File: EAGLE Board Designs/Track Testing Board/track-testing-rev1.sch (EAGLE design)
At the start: 9 parts, among them J1 CONNECTOR-4_μF_S_RA_, U1 VOLTAGE_REGULATOR_SOT-23-5_5V, U2 VOLTAGE_REFERENCE_SOIC-8_10V

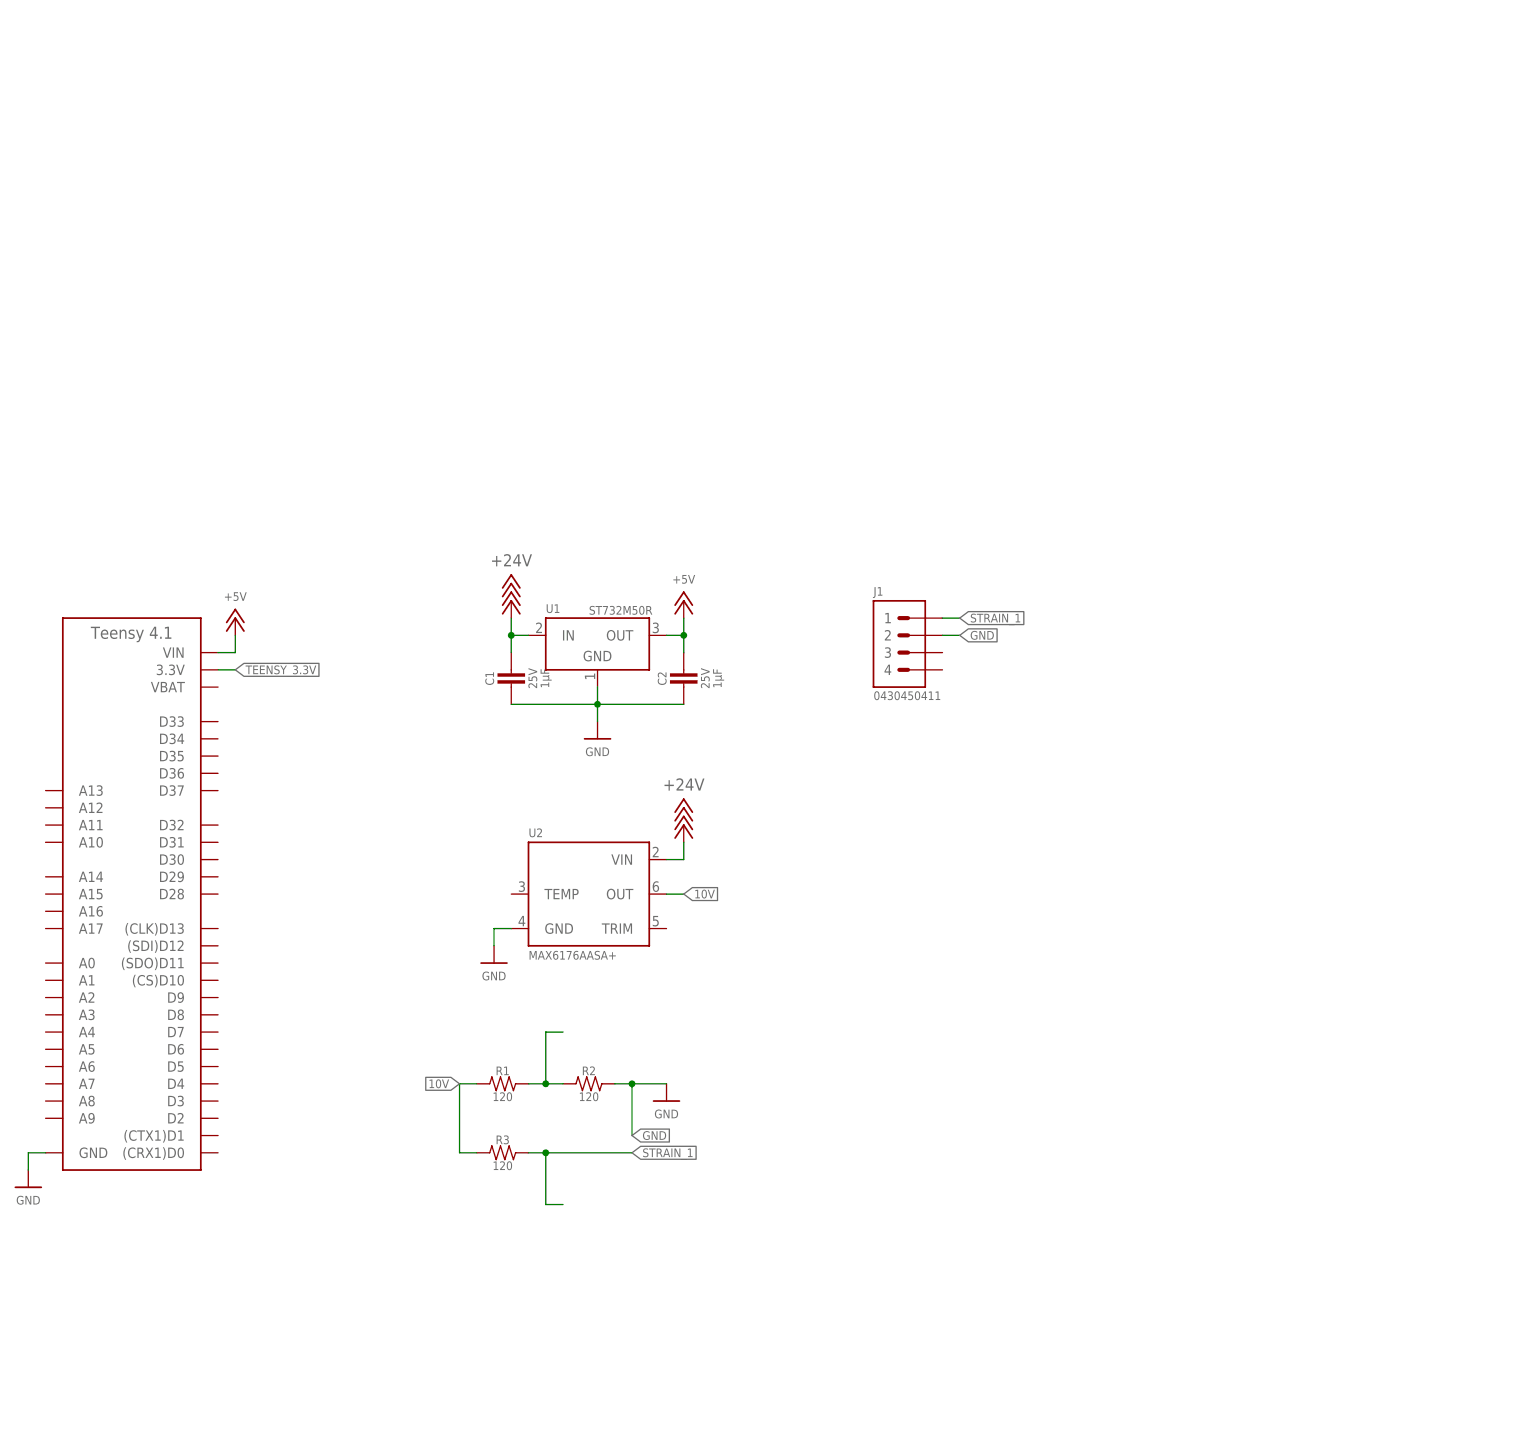
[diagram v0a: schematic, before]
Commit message: enough for two strain gauges
waiting to find datasheet on infrared sensors.
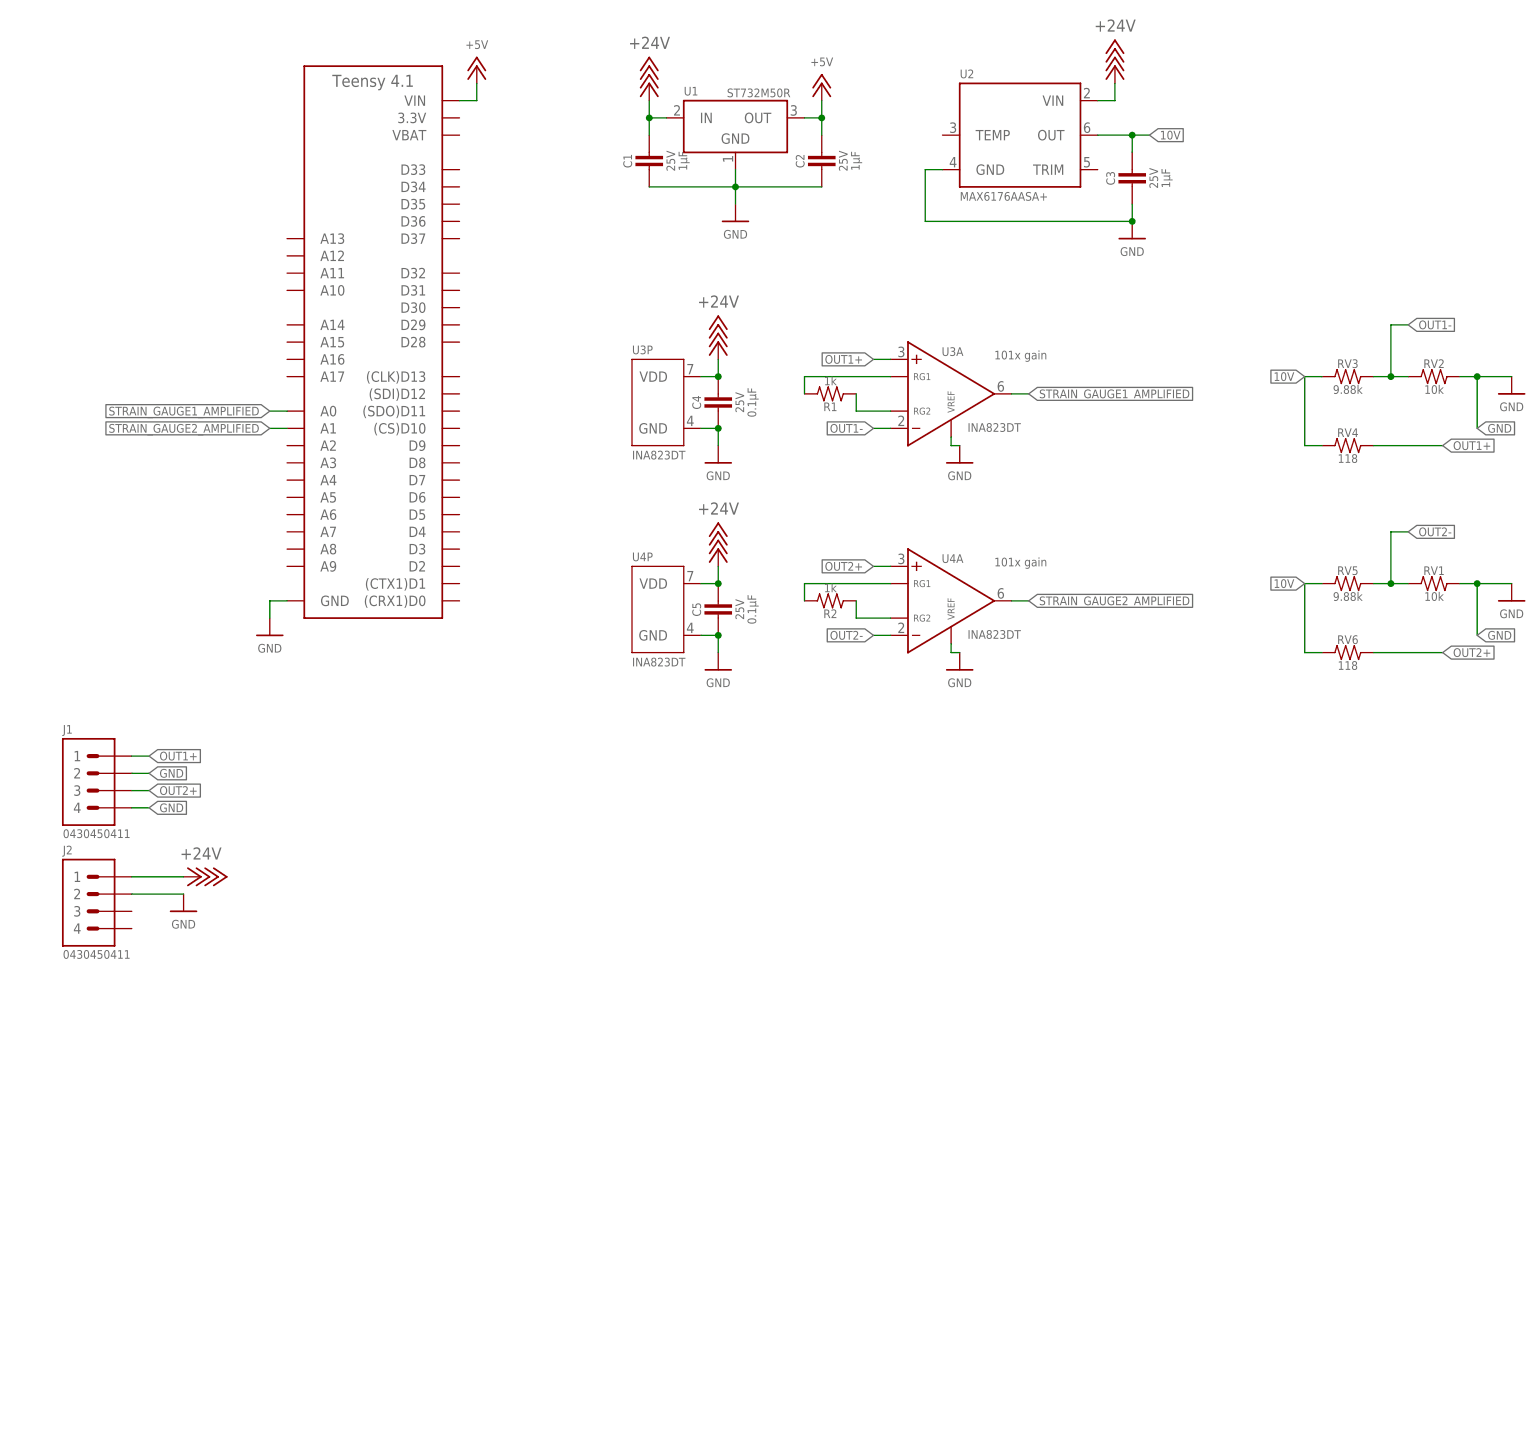
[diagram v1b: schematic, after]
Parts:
- removed R3: RESISTOR_0603_120, HyTechDevices:RESISTOR_0603_120
- added C3: CAPACITOR_0603_25V_1UF, HyTechDevices:CAPACITOR_0603_25V_1UF
- added C4, C5: CAPACITOR_0603_25V_0.1UF, HyTechDevices:CAPACITOR_0603_25V_0.1UF
- added J2: CONNECTOR-4_μF_S_RA_, HyTechDevices:CONNECTOR-4_μF_S_RA_
- added RV1, RV2: 10k, HyTechDevices:RESISTOR_VALUE
- added RV3, RV5: 9.88k, HyTechDevices:RESISTOR_VALUE
- added RV4, RV6: 118, HyTechDevices:RESISTOR_VALUE
- added U3, U4: INA823DT, HyTechDevices:INA823DT
- R1, R2: value RESISTOR_0603_120 -> RESISTOR_0603_1K; device HyTechDevices:RESISTOR_0603_120 -> HyTechDevices:RESISTOR_0603_1K
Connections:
- removed net STRAIN_1: J1.1, R3.2
- removed net TEENSY_3.3V: A1.3.3V
- new net N$1: R2.2, U4A.RG1
- new net N$2: R1.2, U3A.RG1
- new net N$3: R1.1, U3A.RG2
- new net OUT1+: J1.1, RV4.2, U3A.VIN+
- new net OUT1-: RV2.1, RV3.2, U3A.VIN-
- new net OUT2+: J1.3, RV6.2, U4A.VIN+
- new net OUT2-: RV1.1, RV5.2, U4A.VIN-
- new net STRAIN_GAUGE1_AMPLIFIED: A1.A0, U3A.VOUT
- new net STRAIN_GAUGE2_AMPLIFIED: A1.A1, U4A.VOUT
- net +24V: now also C4.1, C5.1, J2.1, U3P.VDD, U4P.VDD
- net 10V: now also C3.1, RV3.1, RV4.1, RV5.1, RV6.1; no longer R1.1, R3.1
- net GND: now also C3.2, C4.2, C5.2, J1.4, J2.2, RV1.2, RV2.2, U3A.VREF, U3P.GND, U4A.VREF, U4P.GND; no longer R2.2
- net N$4: now also U4A.RG2; no longer R1.2
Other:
- note added: "101x gain"
- moved on the sheet: C1, C2, J1, R1, R2, U1, U2

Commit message: passes drc as is
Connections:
- net STRAIN_GAUGE1_AMPLIFIED: now also A1.A1; no longer A1.A0
- net STRAIN_GAUGE2_AMPLIFIED: now also A1.A0; no longer A1.A1
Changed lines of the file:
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@@
 </segment>
 <segment>
-<pinref part="A1" gate="G$1" pin="A0"/>
-<wire x1="43.18" y1="149.86" x2="40.64" y2="149.86" width="0.1524" layer="91"/>
-<label x="40.64" y="149.86" size="1.27" layer="95" rot="R180" xref="yes"/>
+<pinref part="A1" gate="G$1" pin="A1"/>
+<wire x1="43.18" y1="147.32" x2="40.64" y2="147.32" width="0.1524" layer="91"/>
+<label x="40.64" y="147.32" size="1.27" layer="95" rot="R180" xref="yes"/>
 </segment>
 </net>
@@
 </segment>
 <segment>
-<pinref part="A1" gate="G$1" pin="A1"/>
-<wire x1="43.18" y1="147.32" x2="40.64" y2="147.32" width="0.1524" layer="91"/>
-<label x="40.64" y="147.32" size="1.27" layer="95" rot="R180" xref="yes"/>
+<pinref part="A1" gate="G$1" pin="A0"/>
+<wire x1="43.18" y1="149.86" x2="40.64" y2="149.86" width="0.1524" layer="91"/>
+<label x="40.64" y="149.86" size="1.27" layer="95" rot="R180" xref="yes"/>
 </segment>
 </net>

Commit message: 10 strain gauges and aero uart, passes drc
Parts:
- added C10, C11, C12, C13, C6, C7, C8, C9: CAPACITOR_0603_25V_0.1UF, HyTechDevices:CAPACITOR_0603_25V_0.1UF
- added J3, J4: CONNECTOR-4_μF_S_RA_, HyTechDevices:CONNECTOR-4_μF_S_RA_
- added J5: CONNECTOR-10_MF_T_V_, HyTechDevices:CONNECTOR-10_MF_T_V_
- added R10, R3, R4, R5, R6, R7, R8, R9: RESISTOR_0603_1K, HyTechDevices:RESISTOR_0603_1K
- added RV10, RV13, RV16, RV19, RV22, RV25, RV28, RV7: 10k, HyTechDevices:RESISTOR_VALUE
- added RV11, RV14, RV17, RV20, RV23, RV26, RV29, RV8: 9.88k, HyTechDevices:RESISTOR_VALUE
- added RV12, RV15, RV18, RV21, RV24, RV27, RV30, RV9: 118, HyTechDevices:RESISTOR_VALUE
- added U10, U11, U12, U5, U6, U7, U8, U9: INA823DT, HyTechDevices:INA823DT
- J1: value CONNECTOR-4_μF_S_RA_ -> CONNECTOR-10_MF_T_V_; device HyTechDevices:CONNECTOR-4_μF_S_RA_ -> HyTechDevices:CONNECTOR-10_MF_T_V_
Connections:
- new net N$10: R7.2, U9A.RG1
- new net N$11: R4.1, U6A.RG2
- new net N$12: R5.2, U7A.RG1
- new net N$13: R5.1, U7A.RG2
- new net N$14: R7.1, U9A.RG2
- new net N$15: R8.2, U10A.RG1
- new net N$16: R8.1, U10A.RG2
- new net N$17: R9.2, U11A.RG1
- new net N$18: R9.1, U11A.RG2
- new net N$19: R10.2, U12A.RG1
- new net N$20: R10.1, U12A.RG2
- new net N$5: R3.2, U5A.RG1
- new net N$6: R6.2, U8A.RG1
- new net N$7: R3.1, U5A.RG2
- new net N$8: R6.1, U8A.RG2
- new net N$9: R4.2, U6A.RG1
- new net OUT10+: J5.5, RV30.2, U12A.VIN+
- new net OUT10-: RV28.1, RV29.2, U12A.VIN-
- new net OUT3+: J1.3, RV9.2, U5A.VIN+
- new net OUT3-: RV7.1, RV8.2, U5A.VIN-
- new net OUT4+: J1.4, RV12.2, U6A.VIN+
- new net OUT4-: RV10.1, RV11.2, U6A.VIN-
- new net OUT5+: J1.5, RV15.2, U7A.VIN+
- new net OUT5-: RV13.1, RV14.2, U7A.VIN-
- new net OUT6+: J5.1, RV18.2, U8A.VIN+
- new net OUT6-: RV16.1, RV17.2, U8A.VIN-
- new net OUT7+: J5.2, RV21.2, U9A.VIN+
- new net OUT7-: RV19.1, RV20.2, U9A.VIN-
- new net OUT8+: J5.3, RV24.2, U10A.VIN+
- new net OUT8-: RV22.1, RV23.2, U10A.VIN-
- new net OUT9+: J5.4, RV27.2, U11A.VIN+
- new net OUT9-: RV25.1, RV26.2, U11A.VIN-
- new net STRAIN_GAUGE10_AMPLIFIED: A1.A5, U12A.VOUT
- new net STRAIN_GAUGE3_AMPLIFIED: A1.A2, U5A.VOUT
- new net STRAIN_GAUGE4_AMPLIFIED: A1.A1, U6A.VOUT
- new net STRAIN_GAUGE5_AMPLIFIED: A1.A0, U7A.VOUT
- new net STRAIN_GAUGE6_AMPLIFIED: A1.A9, U8A.VOUT
- new net STRAIN_GAUGE7_AMPLIFIED: A1.A8, U9A.VOUT
- new net STRAIN_GAUGE8_AMPLIFIED: A1.A7, U10A.VOUT
- new net STRAIN_GAUGE9_AMPLIFIED: A1.A6, U11A.VOUT
- new net SURREY_RX1: A1.(CTX1)D1, J3.3
- new net SURREY_RX2: A1.D8, J4.3
- new net SURREY_TX1: A1.(CRX1)D0, J3.2
- new net SURREY_TX2: A1.D7, J4.2
- net +24V: now also C10.1, C11.1, C12.1, C13.1, C6.1, C7.1, C8.1, C9.1, U10P.VDD, U11P.VDD, U12P.VDD, U5P.VDD, U6P.VDD, U7P.VDD, U8P.VDD, U9P.VDD
- net +5V: now also J3.1, J4.1
- net 10V: now also RV11.1, RV12.1, RV14.1, RV15.1, RV17.1, RV18.1, RV20.1, RV21.1, RV23.1, RV24.1, RV26.1, RV27.1, RV29.1, RV30.1, RV8.1, RV9.1
- net GND: now also C10.2, C11.2, C12.2, C13.2, C6.2, C7.2, C8.2, C9.2, J1.10, J1.6, J1.7, J1.8, J1.9, J3.4, J4.4, J5.10, J5.6, J5.7, J5.8, J5.9, RV10.2, RV13.2, RV16.2, RV19.2, RV22.2, RV25.2, RV28.2, RV7.2, U10A.VREF, U10P.GND, U11A.VREF, U11P.GND, U12A.VREF, U12P.GND, U5A.VREF, U5P.GND, U6A.VREF, U6P.GND, U7A.VREF, U7P.GND, U8A.VREF, U8P.GND, U9A.VREF, U9P.GND; no longer J1.2, J1.4
- net OUT2+: now also J1.2; no longer J1.3
- net STRAIN_GAUGE1_AMPLIFIED: now also A1.A4; no longer A1.A1
- net STRAIN_GAUGE2_AMPLIFIED: now also A1.A3; no longer A1.A0

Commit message: track testing board
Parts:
- added C14, C17, C18, C54, C55: CAPACITOR_0603_10V_0.1UF, HyTechDevices:CAPACITOR_0603_10V_0.1UF
- added C15, C16, C56, C57: CAPACITOR_0603_10V_1UF, HyTechDevices:CAPACITOR_0603_10V_1UF
- added C19, C20: CAPACITOR_0603_25V_10UF, HyTechDevices:CAPACITOR_0603_25V_10UF
- added J6: CONNECTOR-4_μF_S_RA_, HyTechDevices:CONNECTOR-4_μF_S_RA_
- added R11, R12, R13, R14, R15, R16, R18, R20, R27, R29: RESISTOR_0603_41.2K, HyTechDevices:RESISTOR_0603_41.2K
- added R17, R19, R21, R22, R23, R24, R25, R26, R28, R30: RESISTOR_0603_1K, HyTechDevices:RESISTOR_0603_1K
- added U13, U14, U15, U16, U17, U18, U19, U20, U21, U23: OPAMP_1_CHANNEL_OPA991, HyTechDevices:OPAMP_1_CHANNEL_OPA991
- added U22: ADC128S022, HyTechDevices:ADC128S022
- added U24: TCAN1051HQV-Q1, HyTechDevices:TCAN1051HQV-Q1
- added U25: VOLTAGE_REGULATOR_SOT-223_3.3V, HyTechDevices:VOLTAGE_REGULATOR_SOT-223_3.3V
- added VR1, VR10, VR2, VR3, VR4, VR5, VR6, VR7, VR8, VR9: RESISTOR_TRIMPOT_10K_3362P, HyTechDevices:RESISTOR_TRIMPOT_10K_3362P
- C3: value CAPACITOR_0603_25V_1UF -> CAPACITOR_0603_10V_0.1UF; device HyTechDevices:CAPACITOR_0603_25V_1UF -> HyTechDevices:CAPACITOR_0603_10V_0.1UF
- R1, R10, R2, R3, R4, R5, R6, R7, R8, R9: value RESISTOR_0603_1K -> RESISTOR_0603_402; device HyTechDevices:RESISTOR_0603_1K -> HyTechDevices:RESISTOR_0603_402
- RV1, RV10, RV13, RV16, RV19, RV2, RV22, RV25, RV28, RV7: value 10k -> 1M; device HyTechDevices:RESISTOR_VALUE -> HyTechDevices:RESISTOR_0603_1M
- RV11, RV14, RV17, RV20, RV23, RV26, RV29, RV3, RV5, RV8: value 9.88k -> 1M; device HyTechDevices:RESISTOR_VALUE -> HyTechDevices:RESISTOR_0603_1M
- RV12, RV15, RV18, RV21, RV24, RV27, RV30, RV4, RV6: value 118 -> 120; device HyTechDevices:RESISTOR_VALUE -> HyTechDevices:RESISTOR_0603_120
- RV9: value 118 -> 120
- U2: value VOLTAGE_REFERENCE_SOIC-8_10V -> ADC128S022; device HyTechDevices:VOLTAGE_REFERENCE_SOIC-8_10V -> HyTechDevices:ADC128S022
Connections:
- removed net 10V: C3.1, RV11.1, RV12.1, RV14.1, RV15.1, RV17.1, RV18.1, RV20.1, RV21.1, RV23.1, RV24.1, RV26.1, RV27.1, RV29.1, RV3.1, RV30.1, RV4.1, RV5.1, RV6.1, RV8.1, RV9.1, U2.OUT
- new net !AD1_CS: A1.D33, U2.!CS!
- new net !AD2_CS: A1.D34, U22.!CS!
- new net +3V3: C15.1, C18.1, C20.1, C3.1, C54.1, C56.1, U2.VLOGIC, U22.VLOGIC, U24.VIO, U25.OUT
- new net CANH: J6.3, U24.CANH
- new net CANL: J6.4, U24.CANL
- new net CAN_TT_RX: A1.A9, U24.RXD
- new net CAN_TT_TX: A1.A8, U24.TXD
- new net N$21: R12.2, R22.1, U13A.VIN-
- new net N$22: R11.2, R21.1, U23A.VIN-
- new net N$23: R13.2, R23.1, U14A.VIN-
- new net N$24: R14.2, R24.1, U15A.VIN-
- new net N$25: R15.2, R25.1, U16A.VIN-
- new net N$26: R16.2, R17.1, U17A.VIN-
- new net N$27: R18.2, R19.1, U18A.VIN-
- new net N$28: R20.2, R26.1, U19A.VIN-
- new net N$29: R27.2, R28.1, U20A.VIN-
- new net N$30: R29.2, R30.1, U21A.VIN-
- new net N$41: RV2.1, VR1.1
- new net N$42: RV3.2, VR1.2
- new net N$44: RV1.1, VR2.1
- new net N$45: RV5.2, VR2.2
- new net N$46: RV11.2, VR4.2
- new net N$47: RV7.1, VR3.1
- new net N$48: RV8.2, VR3.2
- new net N$49: RV10.1, VR4.1
- new net N$50: RV14.2, VR5.2
- new net N$51: RV13.1, VR5.1
- new net N$52: RV16.1, VR6.1
- new net N$53: RV17.2, VR6.2
- new net N$54: RV19.1, VR7.1
- new net N$55: RV20.2, VR7.2
- new net N$56: RV22.1, VR8.1
- new net N$57: RV23.2, VR8.2
- new net N$58: RV25.1, VR9.1
- new net N$59: RV26.2, VR9.2
- new net N$60: RV28.1, VR10.1
- new net N$61: RV29.2, VR10.2
- new net STRAIN_GAUGE10_INTER: U12A.VOUT, U21A.VIN+
- new net STRAIN_GAUGE1_INTER: U23A.VIN+, U3A.VOUT
- new net STRAIN_GAUGE2_INTER: U13A.VIN+, U4A.VOUT
- new net STRAIN_GAUGE3_INTER: U14A.VIN+, U5A.VOUT
- new net STRAIN_GAUGE4_INTER: U15A.VIN+, U6A.VOUT
- new net STRAIN_GAUGE5_INTER: U16A.VIN+, U7A.VOUT
- new net STRAIN_GAUGE6_INTER: U17A.VIN+, U8A.VOUT
- new net STRAIN_GAUGE7_INTER: U18A.VIN+, U9A.VOUT
- new net STRAIN_GAUGE8_INTER: U10A.VOUT, U19A.VIN+
- new net STRAIN_GAUGE9_INTER: U11A.VOUT, U20A.VIN+
- new net TT_CLK: A1.(CLK)D13, U2.CLK, U22.CLK
- new net TT_SDI: A1.(SDI)D12, U2.SDO, U22.SDO
- new net TT_SDO: A1.(SDO)D11, U2.SDI, U22.SDI
- net +24V: no longer C10.1, C11.1, C12.1, C13.1, C4.1, C5.1, C6.1, C7.1, C8.1, C9.1, U10P.VDD, U11P.VDD, U12P.VDD, U2.VIN, U3P.VDD, U4P.VDD, U5P.VDD, U6P.VDD, U7P.VDD, U8P.VDD, U9P.VDD
- net +5V: now also C10.1, C11.1, C12.1, C13.1, C14.1, C16.1, C17.1, C19.1, C4.1, C5.1, C55.1, C57.1, C6.1, C7.1, C8.1, C9.1, J6.1, RV11.1, RV12.1, RV14.1, RV15.1, RV17.1, RV18.1, RV20.1, RV21.1, RV23.1, RV24.1, RV26.1, RV27.1, RV29.1, RV3.1, RV30.1, RV4.1, RV5.1, RV6.1, RV8.1, RV9.1, U10P.VDD, U11P.VDD, U12P.VDD, U13P.VDD, U14P.VDD, U15P.VDD, U16P.VDD, U17P.VDD, U18P.VDD, U19P.VDD, U2.AVDD, U20P.VDD, U21P.VDD, U22.AVDD, U23P.VDD, U24.VDD, U25.IN, U3P.VDD, U4P.VDD, U5P.VDD, U6P.VDD, U7P.VDD, U8P.VDD, U9P.VDD
- net GND: now also C14.2, C15.2, C16.2, C17.2, C18.2, C19.2, C20.2, C54.2, C55.2, C56.2, C57.2, J6.2, R17.2, R19.2, R21.2, R22.2, R23.2, R24.2, R25.2, R26.2, R28.2, R30.2, U13P.GND, U14P.GND, U15P.GND, U16P.GND, U17P.GND, U18P.GND, U19P.GND, U2.AGND, U20P.GND, U21P.GND, U22.AGND, U22.GND, U23P.GND, U24.GND, U24.S, U25.GND
- net OUT1+: now also J5.5; no longer J1.1
- net OUT1-: now also VR1.3; no longer RV2.1, RV3.2
- net OUT10+: now also J1.2; no longer J5.5
- net OUT10-: now also VR10.3; no longer RV28.1, RV29.2
- net OUT2+: now also J5.4; no longer J1.2
- net OUT2-: now also VR2.3; no longer RV1.1, RV5.2
- net OUT3+: now also J1.5; no longer J1.3
- net OUT3-: now also VR3.3; no longer RV7.1, RV8.2
- net OUT4-: now also VR4.3; no longer RV10.1, RV11.2
- net OUT5+: now also J1.3; no longer J1.5
- net OUT5-: now also VR5.3; no longer RV13.1, RV14.2
- net OUT6-: now also VR6.3; no longer RV16.1, RV17.2
- net OUT7-: now also VR7.3; no longer RV19.1, RV20.2
- net OUT8-: now also VR8.3; no longer RV22.1, RV23.2
- net OUT9+: now also J1.1; no longer J5.4
- net OUT9-: now also VR9.3; no longer RV25.1, RV26.2
- net STRAIN_GAUGE10_AMPLIFIED: now also R29.1, U21A.VOUT, U22.IN1; no longer A1.A5, U12A.VOUT
- net STRAIN_GAUGE1_AMPLIFIED: now also R11.1, U2.IN0, U23A.VOUT; no longer A1.A4, U3A.VOUT
- net STRAIN_GAUGE2_AMPLIFIED: now also R12.1, U13A.VOUT, U2.IN1; no longer A1.A3, U4A.VOUT
- net STRAIN_GAUGE3_AMPLIFIED: now also R13.1, U14A.VOUT, U2.IN2; no longer A1.A2, U5A.VOUT
- net STRAIN_GAUGE4_AMPLIFIED: now also R14.1, U15A.VOUT, U22.IN6; no longer A1.A1, U6A.VOUT
- net STRAIN_GAUGE5_AMPLIFIED: now also R15.1, U16A.VOUT, U22.IN7; no longer A1.A0, U7A.VOUT
- net STRAIN_GAUGE6_AMPLIFIED: now also R16.1, U17A.VOUT, U2.IN5; no longer A1.A9, U8A.VOUT
- net STRAIN_GAUGE7_AMPLIFIED: now also R18.1, U18A.VOUT, U2.IN6; no longer A1.A8, U9A.VOUT
- net STRAIN_GAUGE8_AMPLIFIED: now also R20.1, U19A.VOUT, U2.IN7; no longer A1.A7, U10A.VOUT
- net STRAIN_GAUGE9_AMPLIFIED: now also R27.1, U20A.VOUT, U22.IN0; no longer A1.A6, U11A.VOUT
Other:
- note added: "42x gain"
